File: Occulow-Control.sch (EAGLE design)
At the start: 17 parts, among them T1 DMP3010LK3, T2 DMP3010LK3, T3 DMP3010LK3

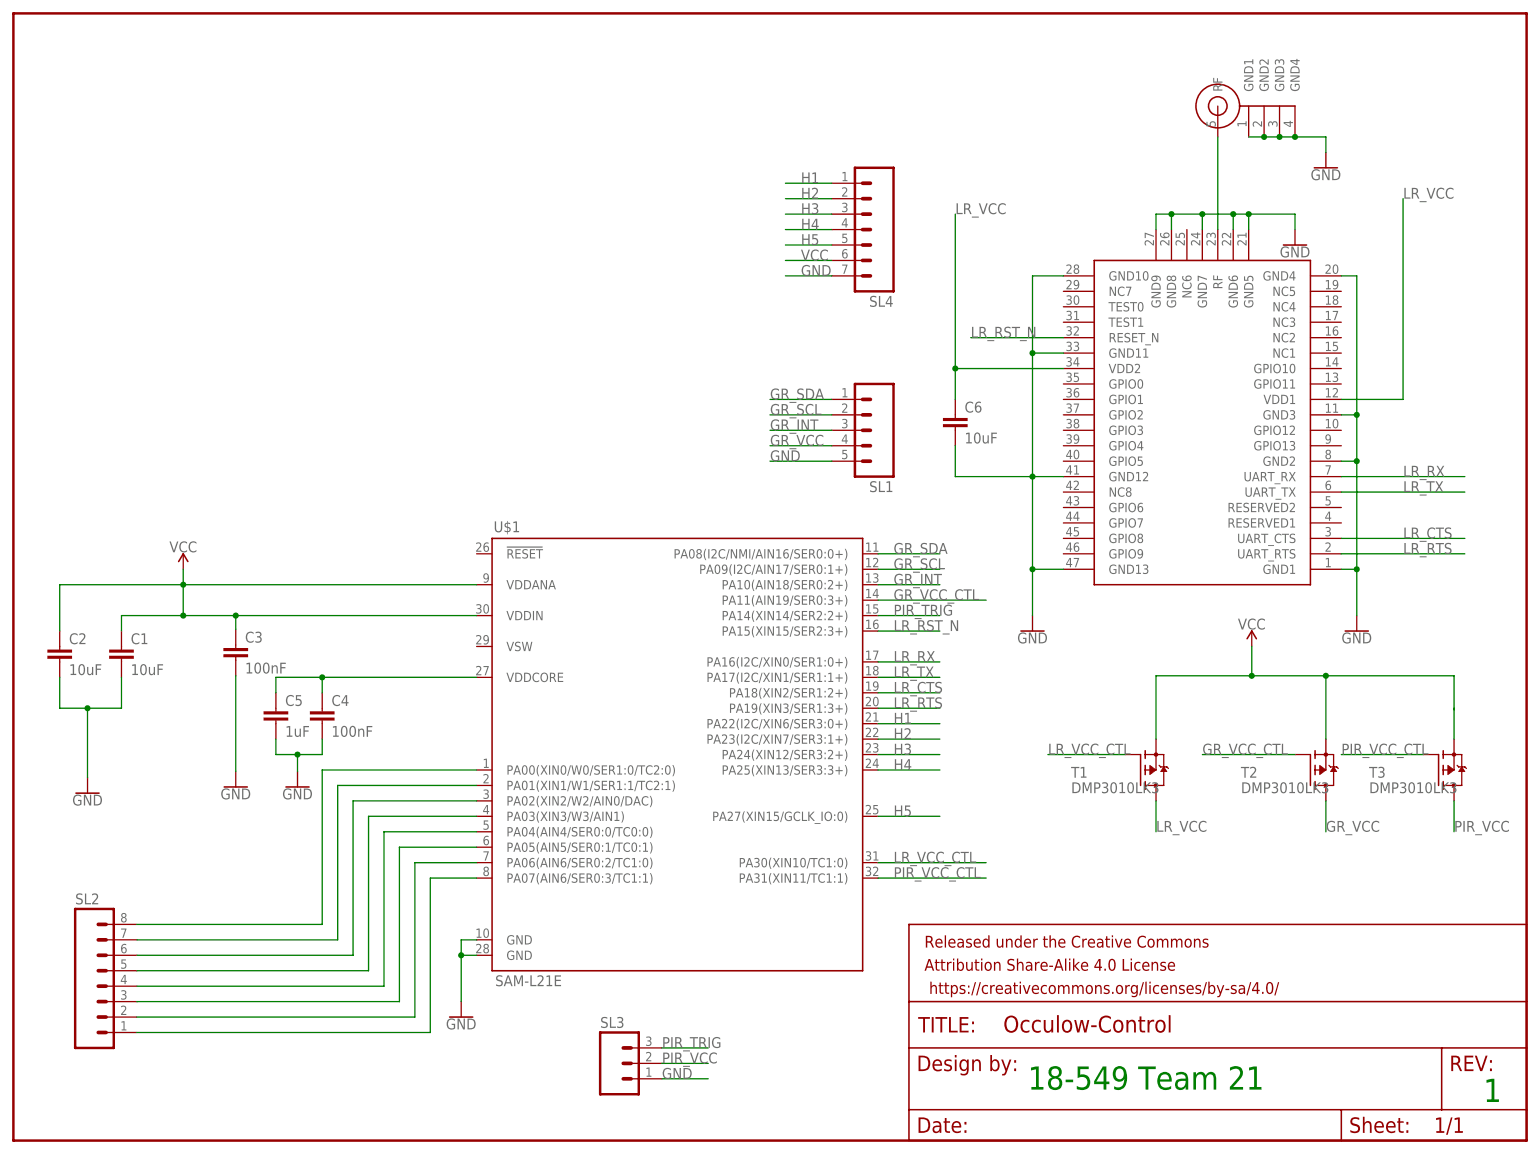
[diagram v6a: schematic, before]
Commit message: Moved header pins around, serial debugger header, JST connector
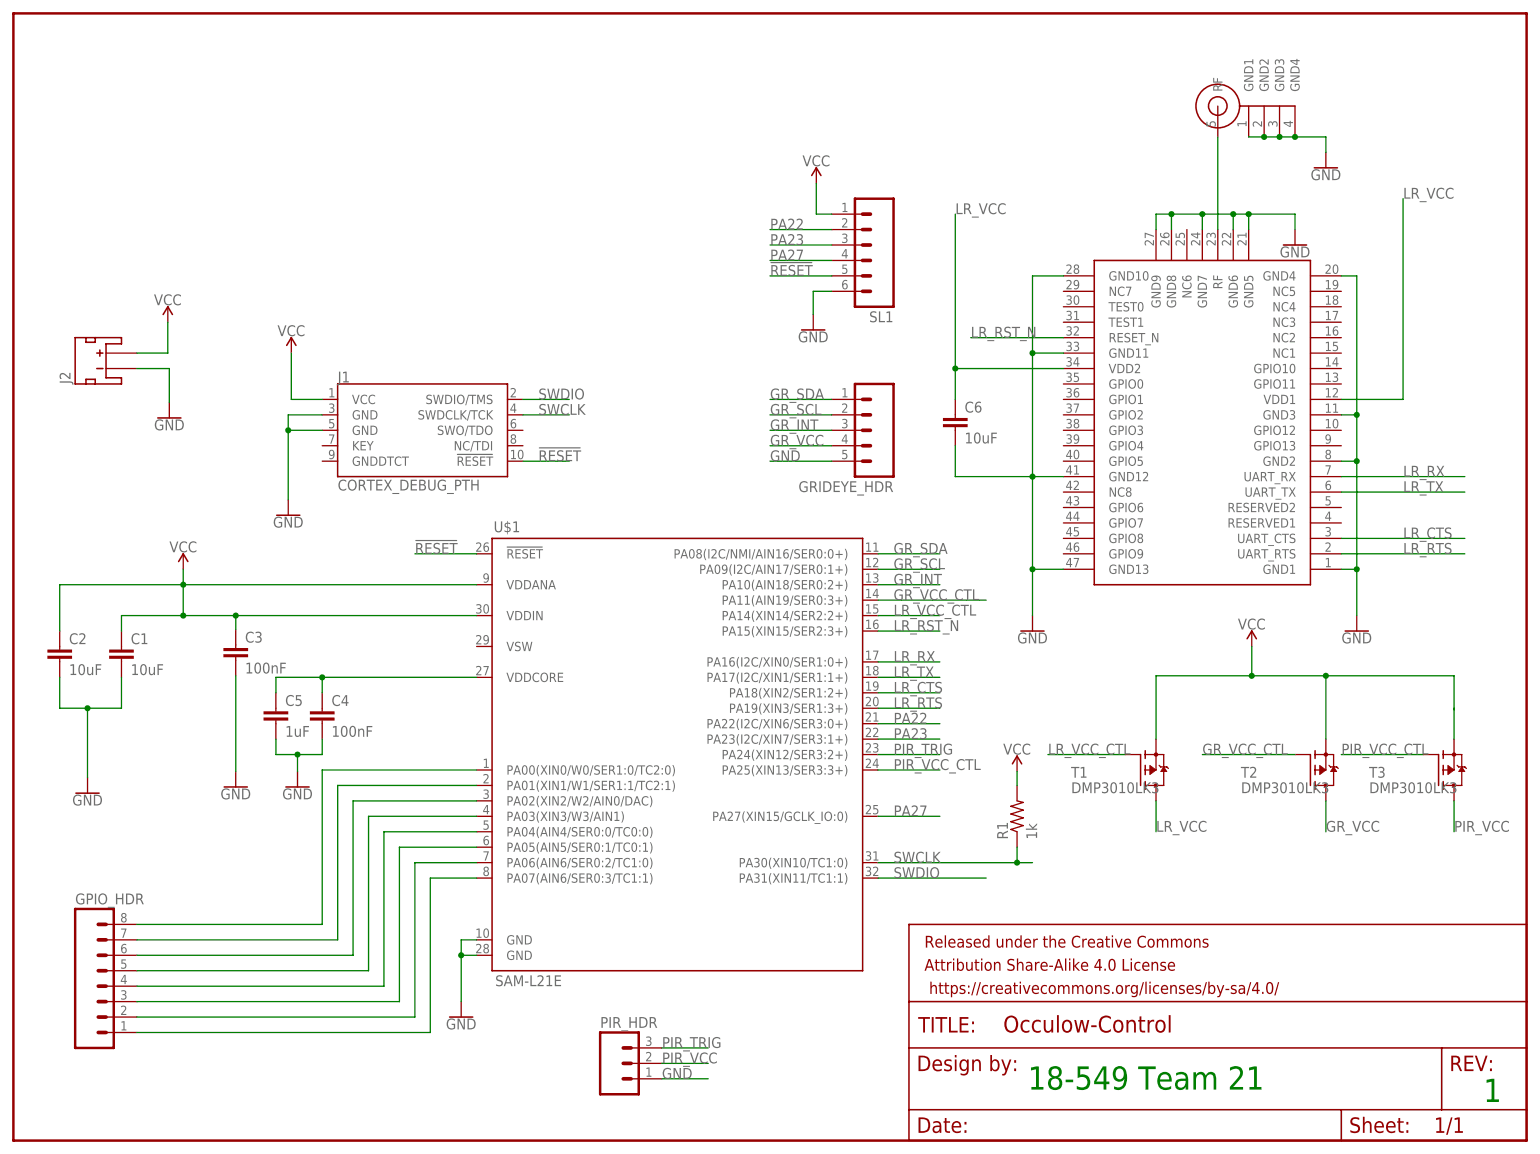
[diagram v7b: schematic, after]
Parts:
- removed SL4: (no value), con-amp-quick:M07
- added GRIDEYE_HDR: (no value), con-amp-quick:M05
- added J1: CORTEX_DEBUG_PTH, SparkFun-Connectors:CORTEX_DEBUG_PTH
- added J2: (no value), SparkFun-Connectors:JST_2MM_MALE
- added R1: 1k, resistor:R-US_R1206
- SL1: device con-amp-quick:M05 -> con-amp-quick:M06
- renumbered SL2 to GPIO_HDR, SL3 to PIR_HDR
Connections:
- removed net H1: SL4.1, U$1.PA22(I2C/XIN6/SER3:0+)
- removed net H2: SL4.2, U$1.PA23(I2C/XIN7/SER3:1+)
- removed net H3: SL4.3, U$1.PA24(XIN12/SER3:2+)
- removed net H4: SL4.4, U$1.PA25(XIN13/SER3:3+)
- removed net H5: SL4.5, U$1.PA27(XIN15/GCLK_IO:0)
- new net !RESET: J1.!RESET, SL1.5, U$1.!RESET
- new net PA22: SL1.2, U$1.PA22(I2C/XIN6/SER3:0+)
- new net PA23: SL1.3, U$1.PA23(I2C/XIN7/SER3:1+)
- new net PA27: SL1.4, U$1.PA27(XIN15/GCLK_IO:0)
- new net SWCLK: J1.SWDCLK/TCK, R1.1, U$1.PA30(XIN10/TC1:0)
- new net SWDIO: J1.SWDIO/TMS, U$1.PA31(XIN11/TC1:1)
- net GND: now also GRIDEYE_HDR.5, J1.GND@3, J1.GND@5, J2.-, SL1.6; no longer SL1.5, SL4.7
- net GR_INT: now also GRIDEYE_HDR.3; no longer SL1.3
- net GR_SCL: now also GRIDEYE_HDR.2; no longer SL1.2
- net GR_SDA: now also GRIDEYE_HDR.1; no longer SL1.1
- net GR_VCC: now also GRIDEYE_HDR.4; no longer SL1.4
- net LR_VCC_CTL: now also U$1.PA14(XIN14/SER2:2+); no longer U$1.PA30(XIN10/TC1:0)
- net PIR_TRIG: now also U$1.PA24(XIN12/SER3:2+); no longer U$1.PA14(XIN14/SER2:2+)
- net PIR_VCC_CTL: now also U$1.PA25(XIN13/SER3:3+); no longer U$1.PA31(XIN11/TC1:1)
- net VCC: now also J1.VCC, J2.+, R1.2, SL1.1; no longer SL4.6

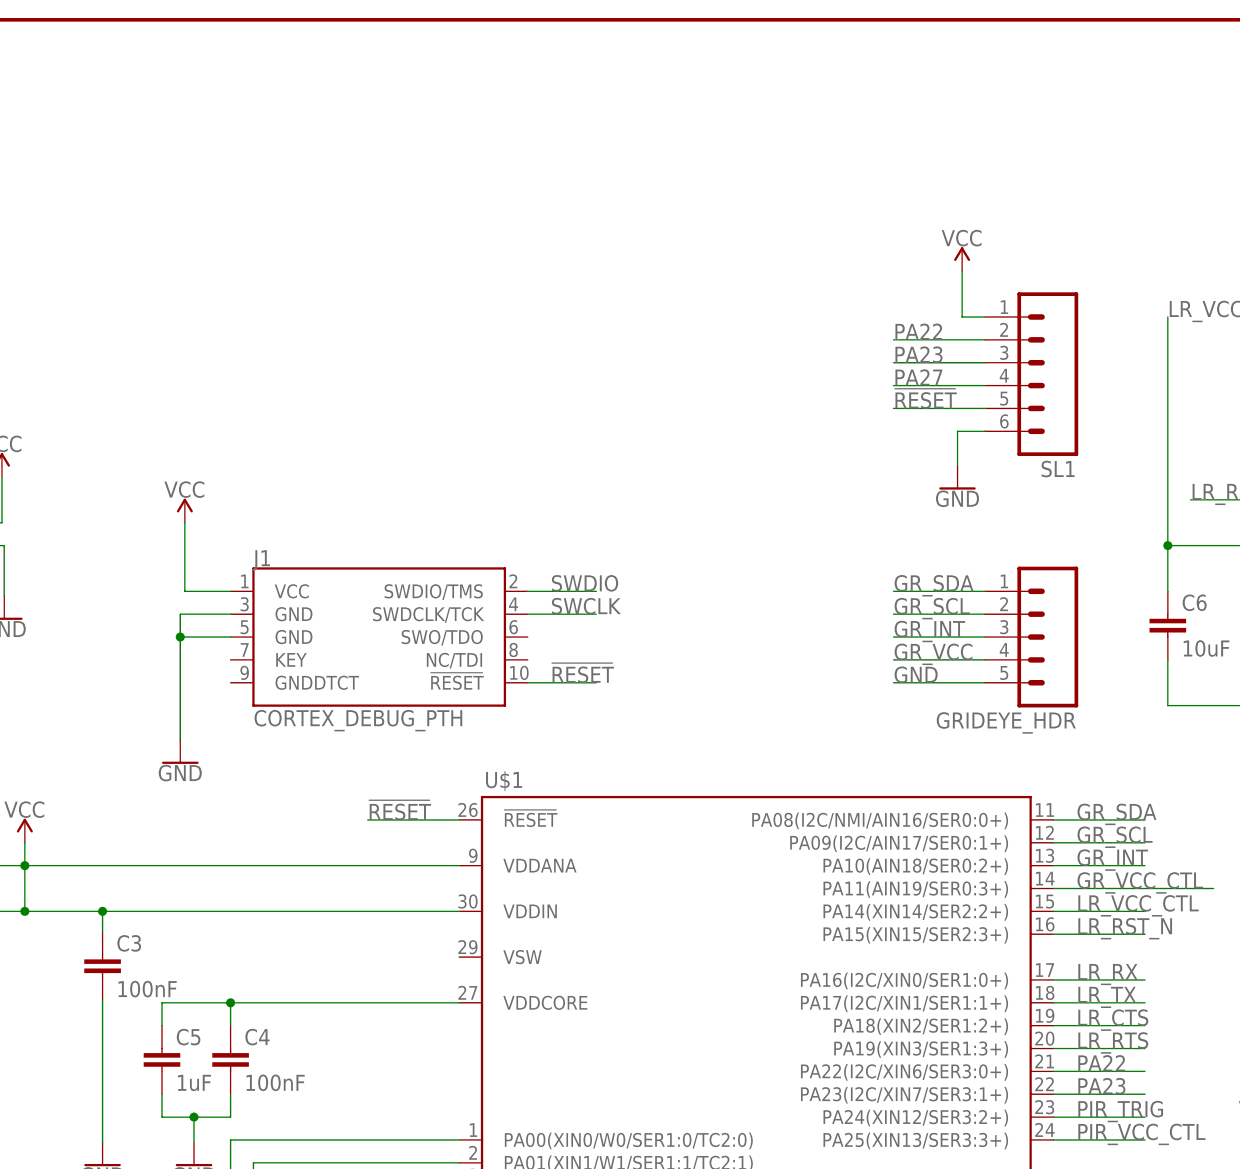
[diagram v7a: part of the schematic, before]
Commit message: Inductor on VSW for switching power mode
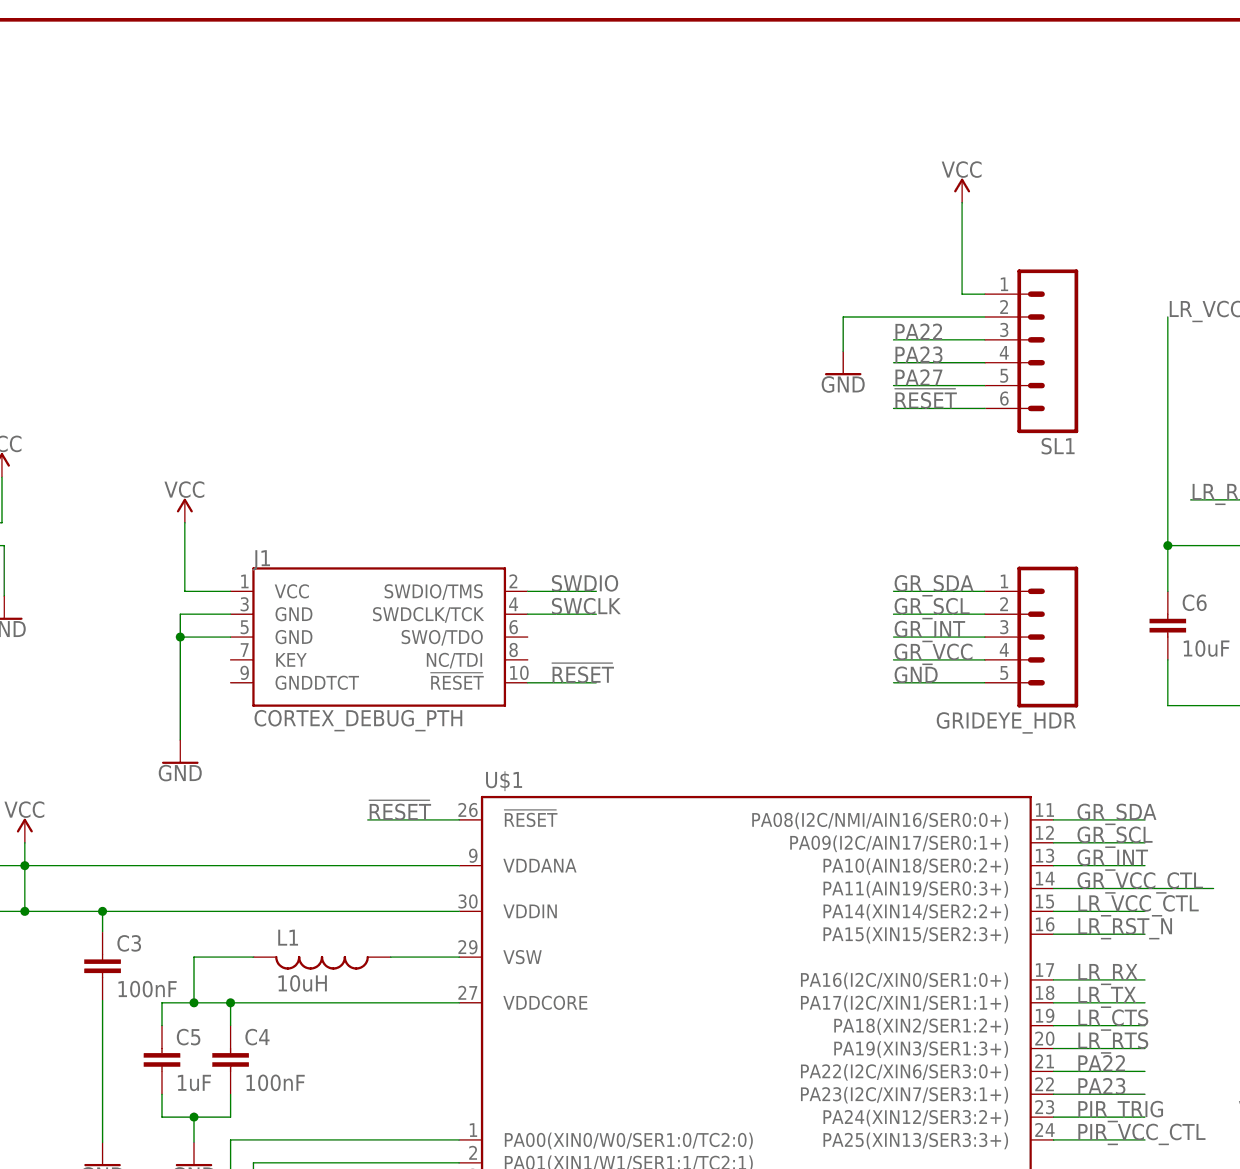
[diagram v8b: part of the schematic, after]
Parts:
- added L1: 10uH, resistor:L-USL2012C
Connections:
- new net N$10: L1.1, U$1.VSW
- net !RESET: now also SL1.6; no longer SL1.5
- net GND: now also SL1.2; no longer SL1.6
- net N$1: now also L1.2
- net PA22: now also SL1.3; no longer SL1.2
- net PA23: now also SL1.4; no longer SL1.3
- net PA27: now also SL1.5; no longer SL1.4
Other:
- moved on the sheet: SL1
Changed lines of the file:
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@@
 <part name="SUPPLY4" library="SparkFun-PowerSymbols" deviceset="VCC" device=""/>
 <part name="GND9" library="SparkFun-PowerSymbols" deviceset="GND" device=""/>
-<part name="SL1" library="con-amp-quick" deviceset="M06" device=""/>
 <part name="SUPPLY5" library="SparkFun-PowerSymbols" deviceset="VCC" device=""/>
 <part name="GND10" library="SparkFun-PowerSymbols" deviceset="GND" device=""/>
@@
 <part name="SUPPLY6" library="SparkFun-PowerSymbols" deviceset="VCC" device=""/>
 <part name="GND11" library="SparkFun-PowerSymbols" deviceset="GND" device=""/>
+<part name="SL1" library="con-amp-quick" deviceset="M06" device=""/>
+<part name="L1" library="resistor" deviceset="L-US" device="L2012C" value="10uH"/>
 </parts>
 <sheets>
@@
 <instance part="SUPPLY4" gate="G$1" x="45.72" y="129.54"/>
 <instance part="GND9" gate="1" x="45.212" y="102.87"/>
-<instance part="SL1" gate="G$1" x="139.7" y="147.32" rot="R180"/>
-<instance part="SUPPLY5" gate="G$1" x="132.08" y="157.48"/>
-<instance part="GND10" gate="1" x="131.572" y="133.35"/>
+<instance part="SUPPLY5" gate="G$1" x="132.08" y="165.1"/>
+<instance part="GND10" gate="1" x="118.872" y="146.05"/>
 <instance part="J2" gate="G$1" x="15.24" y="127" rot="R90"/>
 <instance part="SUPPLY6" gate="G$1" x="25.4" y="134.62"/>
 <instance part="GND11" gate="1" x="25.654" y="118.872"/>
+<instance part="SL1" gate="G$1" x="139.7" y="149.86" rot="R180"/>
+<instance part="L1" gate="G$1" x="60.96" y="81.28" rot="R270"/>
 </instances>
 <busses>
@@
 </segment>
 <segment>
-<pinref part="SL1" gate="G$1" pin="6"/>
-<pinref part="GND10" gate="1" pin="GND"/>
-<wire x1="134.62" y1="139.7" x2="131.572" y2="139.7" width="0.1524" layer="91"/>
-<wire x1="131.572" y1="139.7" x2="131.572" y2="135.89" width="0.1524" layer="91"/>
-</segment>
-<segment>
 <pinref part="J2" gate="G$1" pin="-"/>
 <pinref part="GND11" gate="1" pin="GND"/>
 <wire x1="20.32" y1="127" x2="25.654" y2="127" width="0.1524" layer="91"/>
 <wire x1="25.654" y1="127" x2="25.654" y2="121.412" width="0.1524" layer="91"/>
+</segment>
+<segment>
+<pinref part="SL1" gate="G$1" pin="2"/>
+<pinref part="GND10" gate="1" pin="GND"/>
+<wire x1="134.62" y1="152.4" x2="118.872" y2="152.4" width="0.1524" layer="91"/>
+<wire x1="118.872" y1="152.4" x2="118.872" y2="148.59" width="0.1524" layer="91"/>
 </segment>
 </net>
@@
 </segment>
 <segment>
-<pinref part="SL1" gate="G$1" pin="1"/>
-<pinref part="SUPPLY5" gate="G$1" pin="VCC"/>
-<wire x1="134.62" y1="152.4" x2="132.08" y2="152.4" width="0.1524" layer="91"/>
-<wire x1="132.08" y1="152.4" x2="132.08" y2="157.48" width="0.1524" layer="91"/>
-</segment>
-<segment>
 <pinref part="J2" gate="G$1" pin="+"/>
 <pinref part="SUPPLY6" gate="G$1" pin="VCC"/>
 <wire x1="20.32" y1="129.54" x2="25.4" y2="129.54" width="0.1524" layer="91"/>
 <wire x1="25.4" y1="129.54" x2="25.4" y2="134.62" width="0.1524" layer="91"/>
+</segment>
+<segment>
+<pinref part="SL1" gate="G$1" pin="1"/>
+<pinref part="SUPPLY5" gate="G$1" pin="VCC"/>
+<wire x1="134.62" y1="154.94" x2="132.08" y2="154.94" width="0.1524" layer="91"/>
+<wire x1="132.08" y1="154.94" x2="132.08" y2="165.1" width="0.1524" layer="91"/>
 </segment>
 </net>
@@
 <wire x1="50.8" y1="76.2" x2="50.8" y2="73.66" width="0.1524" layer="91"/>
 <pinref part="C5" gate="G$1" pin="1"/>
-<wire x1="50.8" y1="76.2" x2="43.18" y2="76.2" width="0.1524" layer="91"/>
+<wire x1="50.8" y1="76.2" x2="46.736" y2="76.2" width="0.1524" layer="91"/>
+<wire x1="46.736" y1="76.2" x2="43.18" y2="76.2" width="0.1524" layer="91"/>
 <wire x1="43.18" y1="76.2" x2="43.18" y2="73.66" width="0.1524" layer="91"/>
 <junction x="50.8" y="76.2"/>
+<pinref part="L1" gate="G$1" pin="2"/>
+<wire x1="53.34" y1="81.28" x2="46.736" y2="81.28" width="0.1524" layer="91"/>
+<wire x1="46.736" y1="81.28" x2="46.736" y2="76.2" width="0.1524" layer="91"/>
+<junction x="46.736" y="76.2"/>
 </segment>
 </net>
@@
 </segment>
 <segment>
-<pinref part="SL1" gate="G$1" pin="2"/>
 <wire x1="134.62" y1="149.86" x2="124.46" y2="149.86" width="0.1524" layer="91"/>
 <label x="124.46" y="149.86" size="1.778" layer="95"/>
+<pinref part="SL1" gate="G$1" pin="3"/>
 </segment>
 </net>
@@
 </segment>
 <segment>
-<pinref part="SL1" gate="G$1" pin="3"/>
 <wire x1="134.62" y1="147.32" x2="124.46" y2="147.32" width="0.1524" layer="91"/>
 <label x="124.46" y="147.32" size="1.778" layer="95"/>
+<pinref part="SL1" gate="G$1" pin="4"/>
 </segment>
 </net>
@@
 </segment>
 <segment>
-<pinref part="SL1" gate="G$1" pin="4"/>
 <wire x1="134.62" y1="144.78" x2="124.46" y2="144.78" width="0.1524" layer="91"/>
 <label x="124.46" y="144.78" size="1.778" layer="95"/>
+<pinref part="SL1" gate="G$1" pin="5"/>
 </segment>
 </net>
@@
 </segment>
 <segment>
-<pinref part="SL1" gate="G$1" pin="5"/>
 <wire x1="134.62" y1="142.24" x2="124.46" y2="142.24" width="0.1524" layer="91"/>
 <label x="124.46" y="142.24" size="1.778" layer="95"/>
-</segment>
-</net>
+<pinref part="SL1" gate="G$1" pin="6"/>
+</segment>
+</net>
+<net name="N$10" class="0">
+<segment>
+<pinref part="U$1" gate="G$1" pin="VSW"/>
+<pinref part="L1" gate="G$1" pin="1"/>
+<wire x1="76.2" y1="81.28" x2="68.58" y2="81.28" width="0.1524" layer="91"/>
+</segment>
+</net>
